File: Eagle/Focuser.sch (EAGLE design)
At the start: 28 parts, among them IC1 L7805, IC2 L7805, Q1 IRF540, Q2 IRF540, Q3 IRF540

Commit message: Circuit for commercial version
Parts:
- removed 12V-OUT, JP1: (no value), pinhead:PINHD-1X2
- removed C1, C2: 10uF, rcl:C-EU025-024X044
- removed D1: (no value), diode:DIODE-D-2.5
- removed FUSE2: 2A, fuse:FUSEBLANK_5X20MM
- removed IC1, IC2: L7805, linear:786TV
- removed JP3, JP4, JP5: (no value), SparkFun-Connectors:CONN_025MM
- removed Q1, Q2, Q3: IRF540, transistor-power:IRF540
- removed R2, R3, R4: 4.7K, rcl:R-EU_0204/5
- removed R5: (no value), pot:TRIM_EU-B64Y
- removed R6: 220R, resistor:R-EU_0204/5
- removed USB1: FEMALE A, Seeed-Connector:DIP-USB-A-TYPE-FMAL(4+2P-2.0-90D)
- FUSE1: value 1.5A -> 1A
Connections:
- removed net D3: Q3.G, R2.2, U$1.D3
- removed net D5: Q2.G, R4.2, U$1.D5
- removed net D6: Q1.G, R3.2, U$1.D6
- removed net N$10: JP4.2, Q1.D
- removed net N$11: JP5.2, Q3.D
- removed net N$19: JP1.1, R6.1
- removed net N$2: R5.S, U$1.A7
- removed net N$3: R6.2, U$1.D11
- removed net N$4: C1.1, FUSE1.2, IC1.VI, IC2.VI
- removed net N$8: 12V-OUT.2, FUSE1.1, FUSE2.1, VIN.2
- removed net N$9: D1.A, JP3.2, Q2.D
- new net N$7: FUSE1.1, VIN.2
- net +12V: now also FUSE1.2, U$1.RAW; no longer D1.C, FUSE2.2, JP3.1, JP4.1, JP5.1
- net +5V: no longer C2.1, IC1.VO, IC2.VO, R5.A, USB1G$1.1
- net GND: no longer 12V-OUT.1, C1.2, C2.2, IC1.GND, IC2.GND, JP1.2, Q1.S, Q2.S, Q3.S, R2.1, R3.1, R4.1, R5.E, U$1.GND2, USB1G$1.4
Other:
- moved on the sheet: C3, DRV1, FUSE1, JP2, LED1, R1, VIN

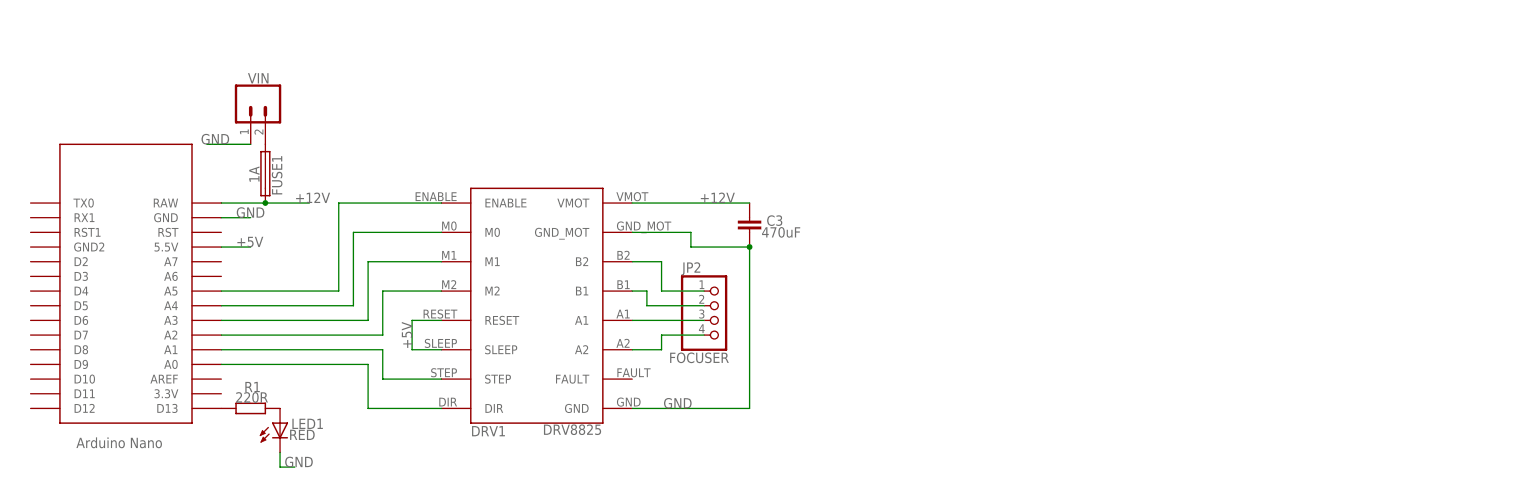
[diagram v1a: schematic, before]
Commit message: Hand control added in circuit
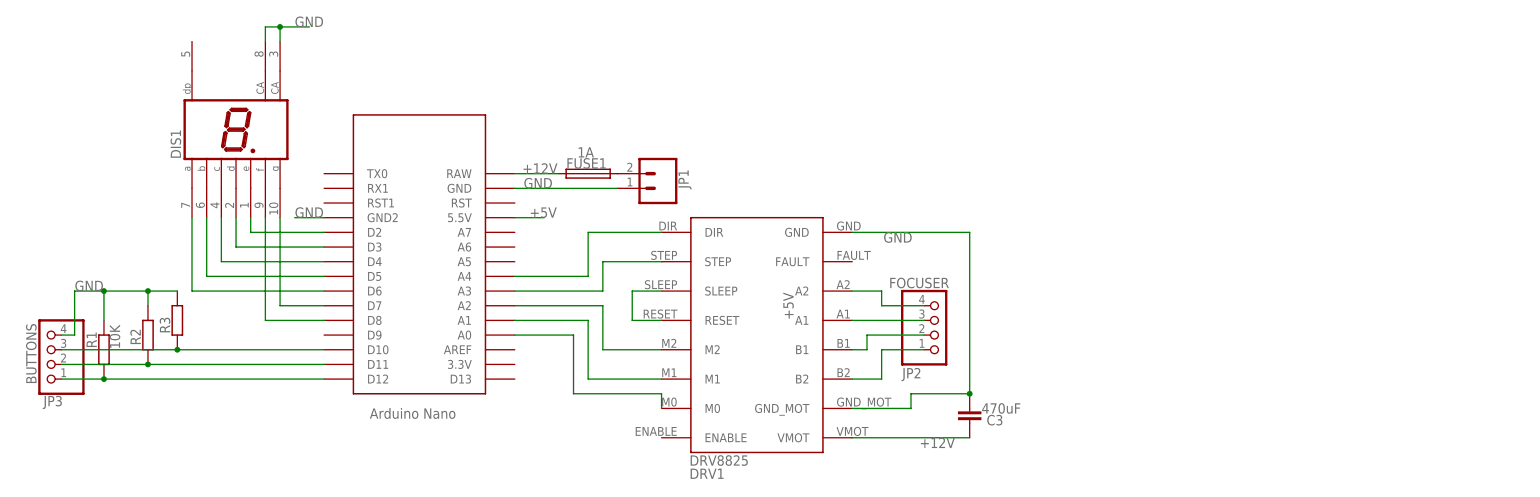
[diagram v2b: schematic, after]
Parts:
- removed LED1: RED, adafruit:LED3MM
- removed VIN: (no value), SparkFun-Connectors:CONN_025MM
- added DIS1: HD-H101, display-hp:HD-H101
- added JP1: (no value), SparkFun-Connectors:CONN_025MM
- added JP3: BUTTONS, pinhead:PINHD-1X4
- added R2, R3: 10K, resistor:R-EU_0204/2V
- FUSE1: SPICEPREFIX (none) -> F
- R1: value 220R -> 10K; device resistor:R-EU_0204/5 -> resistor:R-EU_0204/2V
- U$1: SPICEPREFIX (none) -> X
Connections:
- removed net D13: R1.2, U$1.D13
- new net N$10: DIS1.A, U$1.D6
- new net N$11: DIS1.G, U$1.D7
- new net N$19: DIS1.F, U$1.D8
- new net N$2: JP3.3, R3.1, U$1.D10
- new net N$3: JP3.2, R2.1, U$1.D11
- new net N$4: JP3.1, R1.1, U$1.D12
- new net N$8: DIS1.C, U$1.D4
- new net N$9: DIS1.B, U$1.D5
- net GND: now also DIS1.CA, DIS1.CA@1, JP1.1, JP3.4, R1.2, R2.2, R3.2, U$1.GND2; no longer LED1.C, VIN.1
- net N$1: now also DIS1.E, U$1.D2; no longer LED1.A, R1.1
- net N$12: now also U$1.A3; no longer U$1.A1
- net N$18: now also U$1.A1; no longer U$1.A3
- net N$20: now also U$1.A0; no longer U$1.A4
- net N$5: now also U$1.A4; no longer U$1.A0
- net N$6: now also DIS1.D, U$1.D3; no longer DRV1.ENABLE, U$1.A5
- net N$7: now also JP1.2; no longer VIN.2
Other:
- moved on the sheet: C3, DRV1, FUSE1, JP2, R1
